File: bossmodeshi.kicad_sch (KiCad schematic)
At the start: 53 parts, among them Q1 PSMN3R7-100BSE, Q2 PSMN020-100YS, Q4 NPN_REGIN, U1 MP2790DFP-0000-T

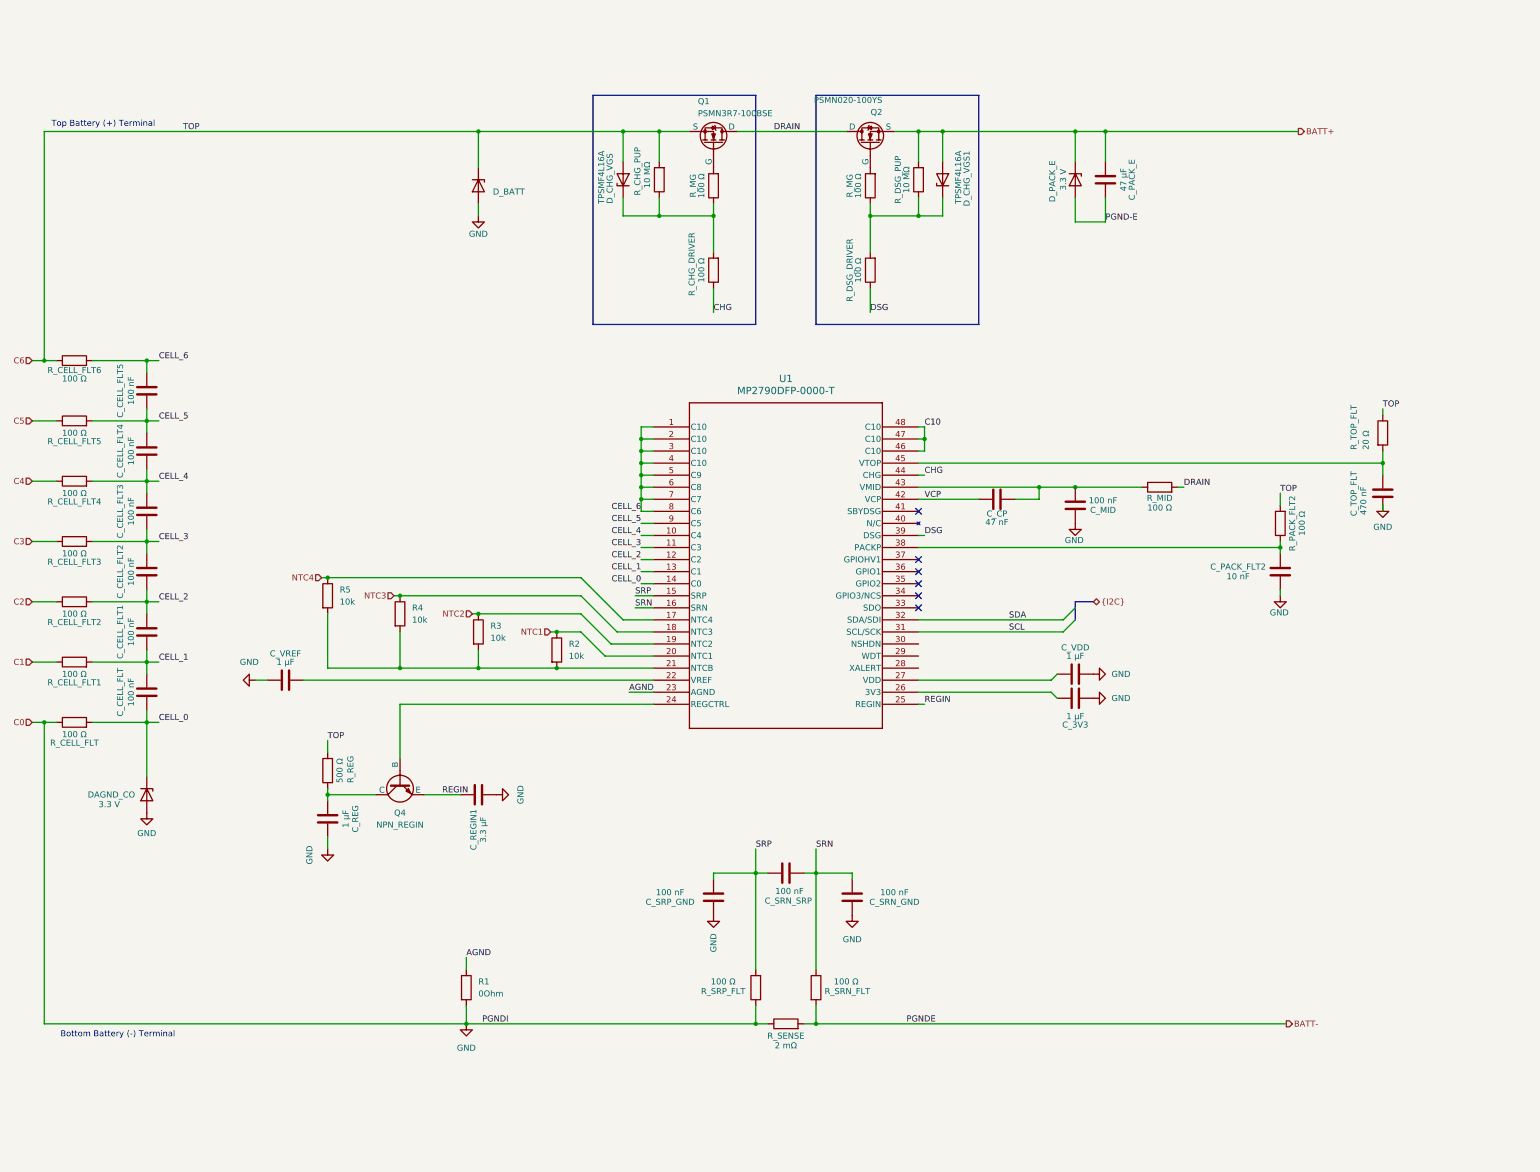
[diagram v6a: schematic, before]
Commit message: added external mosfets
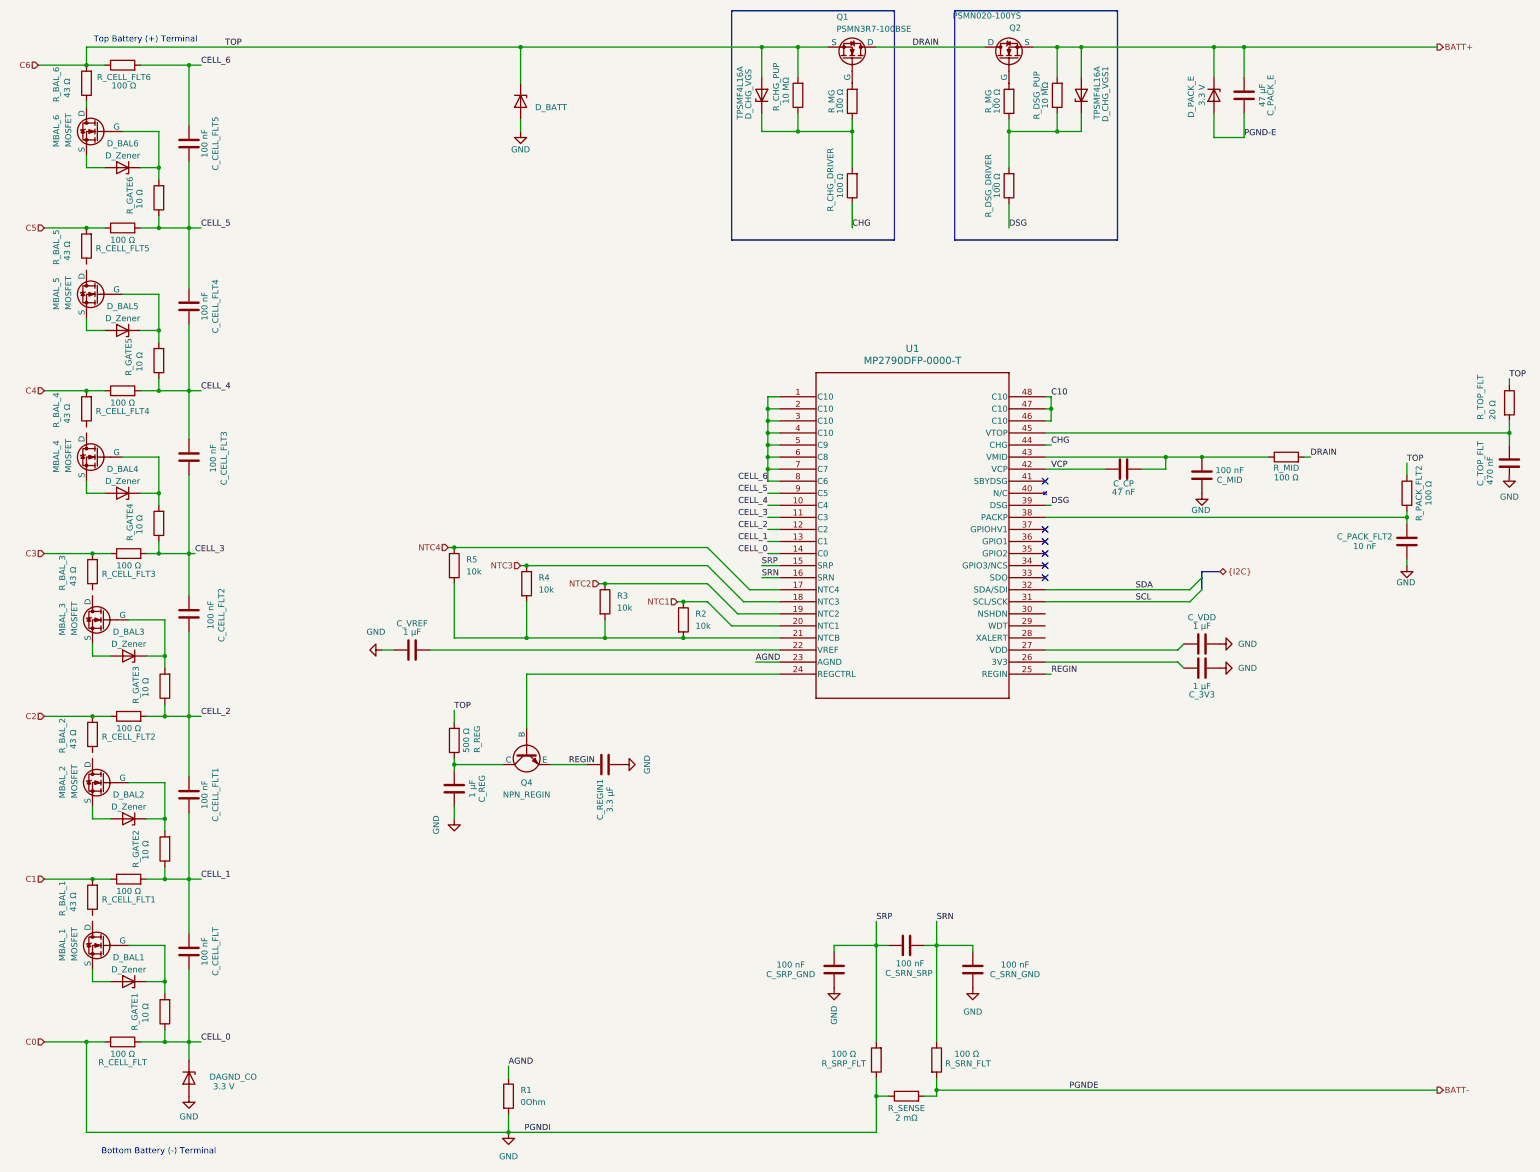
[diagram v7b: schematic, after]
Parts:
- added D_BAL1, D_BAL2, D_BAL3, D_BAL4, D_BAL5, D_BAL6: D_Zener, symbol Device:D_Zener
- added MBAL_1, MBAL_2, MBAL_3, MBAL_4, MBAL_5, MBAL_6: MOSFET, symbol Simulation_SPICE:NMOS
- added R_BAL_1, R_BAL_2, R_BAL_3, R_BAL_4, R_BAL_5, R_BAL_6: 43 Ω, symbol Device:R
- added R_GATE1, R_GATE2, R_GATE3, R_GATE4, R_GATE5, R_GATE6: 10 Ω, symbol Device:R
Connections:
- net C1: now also R_BAL_1.2
- net C2: now also R_BAL_2.2
- net C3: now also R_BAL_3.2
- net C4: now also R_BAL_4.2
- net C5: now also R_BAL_5.2
- net C6: now also R_BAL_6.2
- net CELL_0: now also C_CELL_FLT.2, R_GATE1.1; no longer C_CELL_FLT.1
- net CELL_1: now also C_CELL_FLT.1, C_CELL_FLT1.2, R_GATE2.1; no longer C_CELL_FLT.2, C_CELL_FLT1.1
- net CELL_2: now also C_CELL_FLT1.1, R_GATE3.1; no longer C_CELL_FLT1.2
- net CELL_3: now also R_GATE4.1
- net CELL_4: now also C_CELL_FLT4.2, R_GATE5.1; no longer C_CELL_FLT4.1
- net CELL_5: now also C_CELL_FLT4.1, C_CELL_FLT5.2, R_GATE6.1; no longer C_CELL_FLT4.2, C_CELL_FLT5.1
- net CELL_6: now also C_CELL_FLT5.1; no longer C_CELL_FLT5.2
- new net: D_BAL4.1 (K), MBAL_4.2 (G), R_GATE4.2
- new net: D_BAL4.2 (A), MBAL_4.3 (S)
- new net: D_BAL3.1 (K), MBAL_3.2 (G), R_GATE3.2
- new net: D_BAL1.1 (K), MBAL_1.2 (G), R_GATE1.2
- new net: D_BAL5.1 (K), MBAL_5.2 (G), R_GATE5.2
- new net: D_BAL2.1 (K), MBAL_2.2 (G), R_GATE2.2
- new net: D_BAL2.2 (A), MBAL_2.3 (S)
- new net: D_BAL1.2 (A), MBAL_1.3 (S)
- new net: D_BAL5.2 (A), MBAL_5.3 (S)
- new net: D_BAL3.2 (A), MBAL_3.3 (S)
- new net: MBAL_6.1 (D), R_BAL_6.1
- new net: D_BAL6.1 (K), MBAL_6.2 (G), R_GATE6.2
- new net: D_BAL6.2 (A), MBAL_6.3 (S)
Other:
- moved on the sheet: C_3V3, C_CELL_FLT, C_CELL_FLT1, C_CELL_FLT2, C_CELL_FLT3, C_CELL_FLT4, C_CELL_FLT5, C_CP, C_MID, C_PACK_E, C_PACK_FLT2, C_REG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

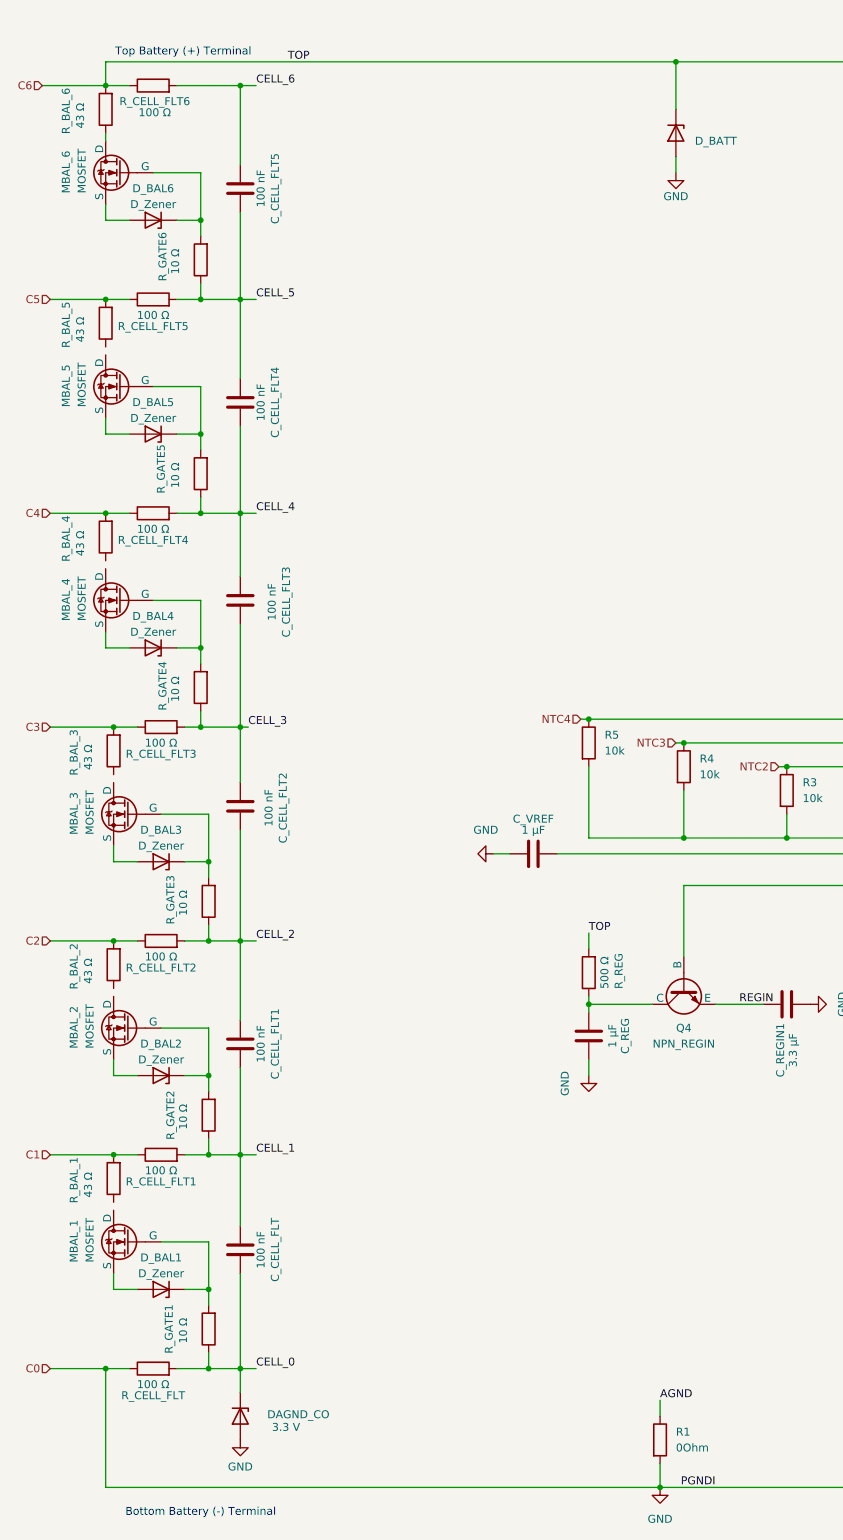
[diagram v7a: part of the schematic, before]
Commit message: added footprints
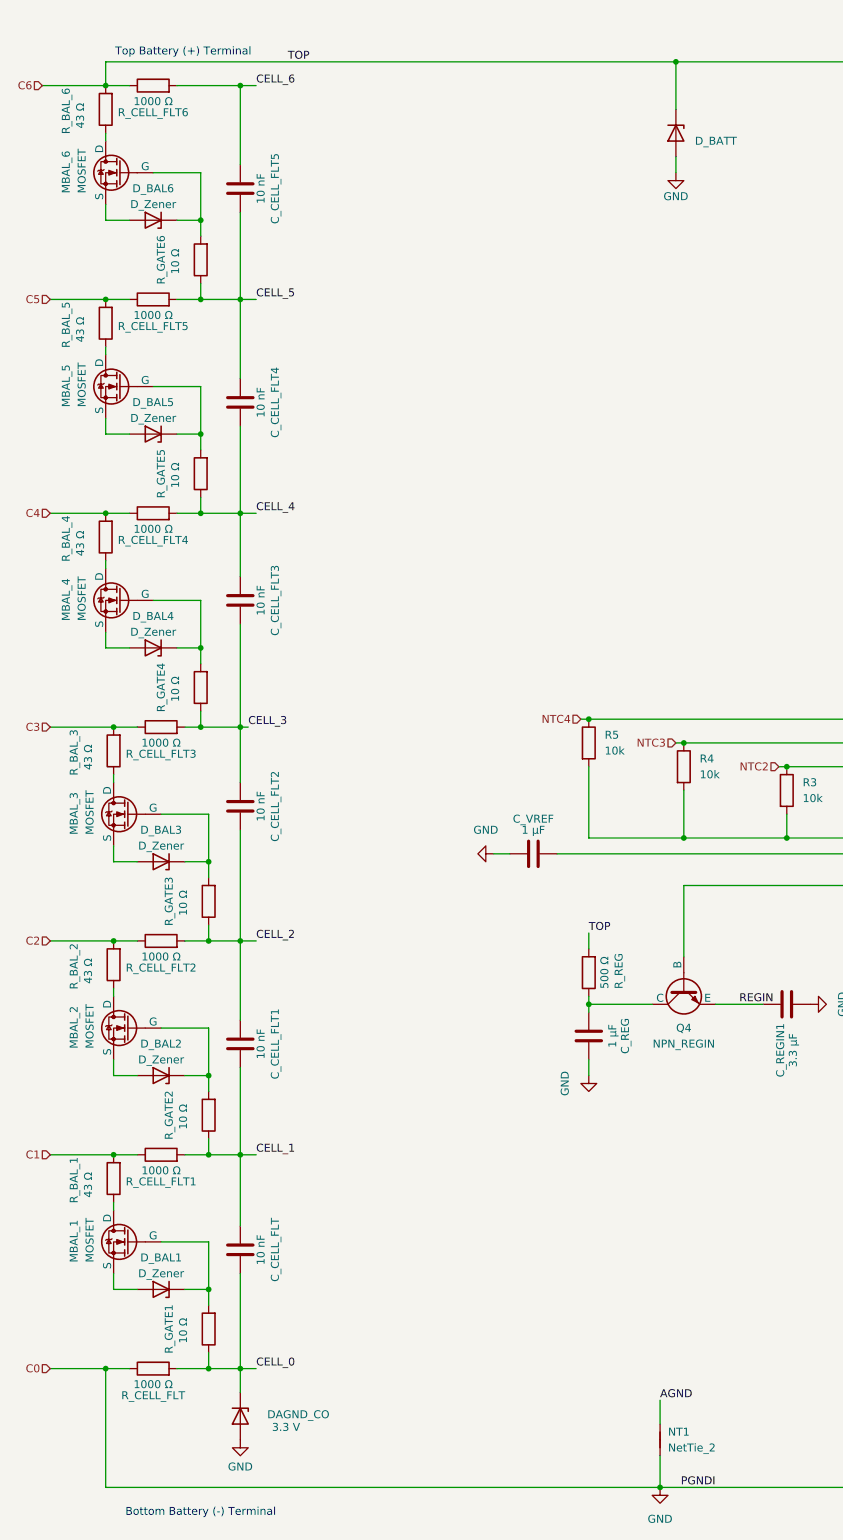
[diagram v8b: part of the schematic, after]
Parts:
- removed R1: 0Ohm, symbol Device:R
- added NT1: NetTie_2, symbol Device:NetTie_2
- C_3V3, C_TOP_FLT, C_VDD: footprint (none) -> Capacitor_SMD:C_0805_2012Metric
- C_CELL_FLT, C_CELL_FLT1, C_CELL_FLT2, C_CELL_FLT3, C_CELL_FLT4, C_CELL_FLT5: value 100 nF -> 10 nF; footprint (none) -> Capacitor_SMD:C_0603_1608Metric; MFR Murata Electronics -> KEMET; MFR P/N GCM31C5C1H104FA16L -> C0603X103F5JACTU; Supplier_1 P/N 490-GCM31C5C1H104FA16LTR-ND -> 399-13405-2-ND; Supplier_1 Price @ QTY 0.98 -> 1; Supplier_1 Unit Price 1 -> 0.93
- C_CP, C_MID, C_PACK_E: footprint (none) -> Capacitor_SMD:C_1206_3216Metric
- C_PACK_FLT2: footprint (none) -> Capacitor_SMD:C_0603_1608Metric
- MBAL_1, MBAL_2, MBAL_3, MBAL_4, MBAL_5, MBAL_6: footprint (none) -> _BMS:SC70-6; MFR (none) -> Vishay Siliconix; MFR P/N (none) -> SQ1464EEH-T1_GE3; Supplier_1 P/N (none) -> SQ1464EEH-T1_GE3TR-ND; Supplier_1 Unit Price (none) -> 0.62
- R2, R3, R4, R5, R_CHG_DRIVER, R_DSG_DRIVER, R_MG, R_MID, R_PACK_FLT2, R_TOP_FLT: footprint (none) -> Resistor_SMD:R_0603_1608Metric
- R_BAL_1, R_BAL_2, R_BAL_3, R_BAL_4, R_BAL_5, R_BAL_6: footprint (none) -> Resistor_SMD:R_2512_6332Metric; MFR (none) -> YAGEO; MFR P/N (none) -> RC2512FK-0743RL; Supplier_1 P/N (none) -> 13-RC2512FK-0743RLTR-ND; Supplier_1 Unit Price (none) -> 0.21
- R_CELL_FLT, R_CELL_FLT1, R_CELL_FLT2, R_CELL_FLT3, R_CELL_FLT4, R_CELL_FLT5, R_CELL_FLT6: value 100 Ω -> 1000 Ω; footprint (none) -> Resistor_SMD:R_0603_1608Metric; MFR Susumu -> Panasonic Electronic Components; MFR P/N RG1608P-101-B-T5 -> ERA-3AEB102V; Supplier_1 P/N RG16P100BTR-ND -> P1.0KDBTR-ND; Supplier_1 Price @ QTY 0.10 -> 1; Supplier_1 Unit Price 1 -> 0.1
- R_CHG_PUP, R_DSG_PUP: footprint (none) -> Resistor_SMD:R_1206_3216Metric
- R_GATE1, R_GATE2, R_GATE3, R_GATE4, R_GATE5, R_GATE6: footprint (none) -> Resistor_SMD:R_0603_1608Metric; MFR (none) -> Stackpole Electronics Inc; MFR P/N (none) -> RNCE0603BTE10R0; Supplier_1 P/N (none) -> 738-RNCE0603BTE10R0TR-ND; Supplier_1 Unit Price (none) -> 0.12
- R_SENSE: footprint (none) -> Resistor_SMD:R_0805_2012Metric; MFR (none) -> YAGEO; MFR P/N (none) -> PA0805FRE7W0R002L; Supplier_1 (none) -> DigiKey; Supplier_1 P/N (none) -> 13-PA0805FRE7W0R002LTR-ND; Supplier_1 Price @ QTY (none) -> 1; Supplier_1 Unit Price (none) -> 0.19
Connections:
- net AGND: now also NT1.2
- net CELL_2: now also C_CELL_FLT2.2; no longer C_CELL_FLT2.1
- net CELL_3: now also C_CELL_FLT2.1, C_CELL_FLT3.2; no longer C_CELL_FLT2.2, C_CELL_FLT3.1
- net CELL_4: now also C_CELL_FLT3.1; no longer C_CELL_FLT3.2
- net GND: now also NT1.1
- net at MBAL_4.1 (D): now also R_BAL_4.1
- net at R_BAL_2.1: now also MBAL_2.1 (D)
- net at R_BAL_3.1: now also MBAL_3.1 (D)
- net at MBAL_5.1 (D): now also R_BAL_5.1
- net at R_BAL_1.1: now also MBAL_1.1 (D)
